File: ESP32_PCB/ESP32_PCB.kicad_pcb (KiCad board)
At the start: 2 copper layers, 40 x 40 mm, 30 parts, among them J1 USB_C_Receptacle, J2 ESC1, J3 ESC2, U2 H3LIS331DL, U3 AP2112K-3.3, U4 TPS54302, U5 ESP32-S3-MINI-1U

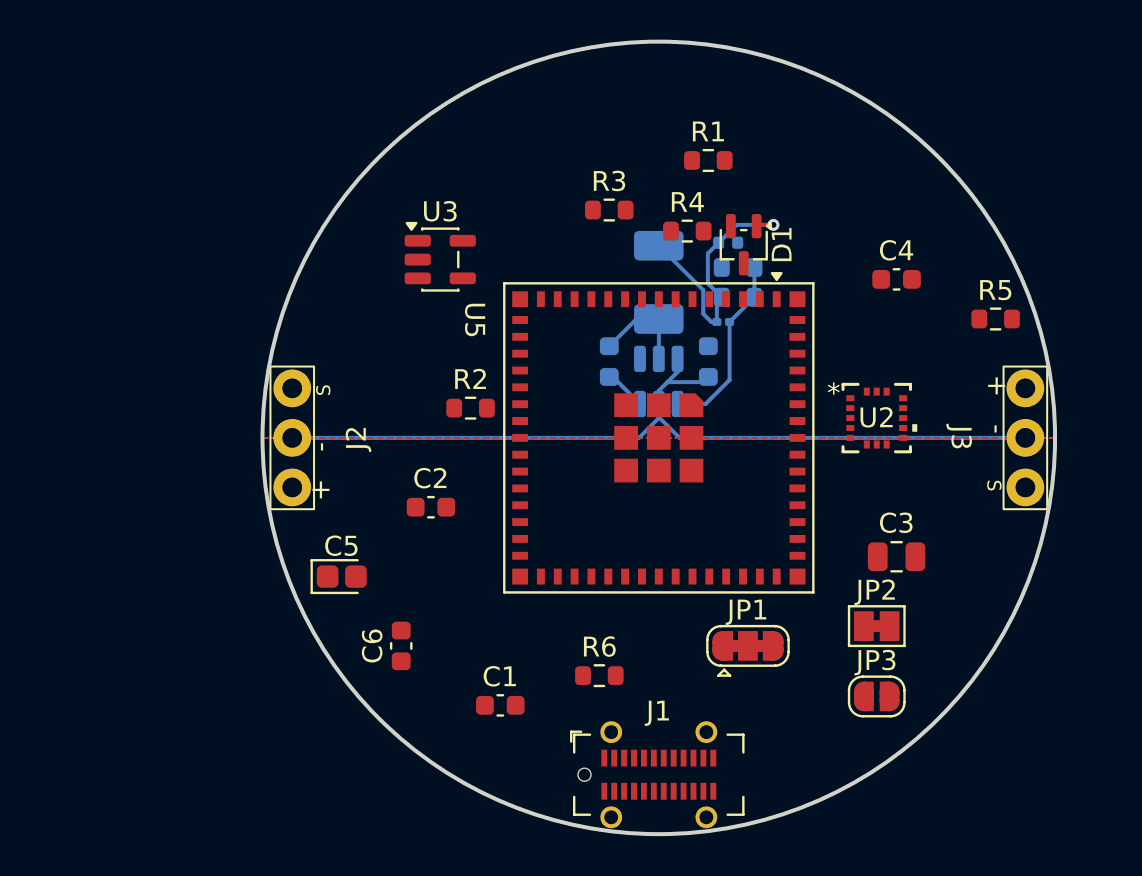
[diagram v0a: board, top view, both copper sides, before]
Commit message: fix pin assignments and add en and boot jumper
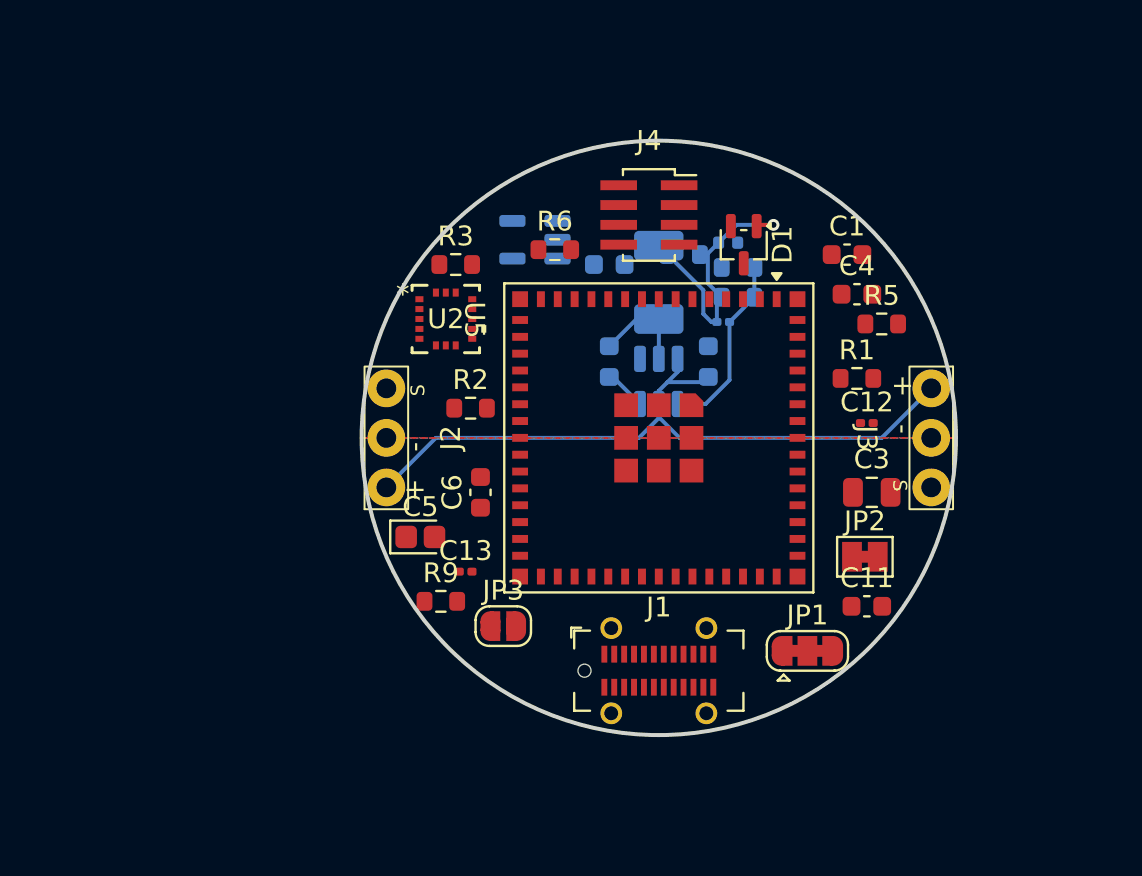
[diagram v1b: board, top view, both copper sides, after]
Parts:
- added C11: 22uF, Capacitor_SMD:C_0603_1608Metric, F.Cu at (160.5, 108.5)
- added C12: 1uF, Capacitor_SMD:C_0201_0603Metric, F.Cu at (160.5, 99.2)
- added C13: 0.1uF, Capacitor_SMD:C_0201_0603Metric, F.Cu at (140.2, 106.8)
- added J4: Conn_02x04_Counter_Clockwise, Connector_PinSocket_1.00mm:PinSocket_2x04_P1.00mm_Vertical_SMD, F.Cu at (149.5, 88.8)
- added R9: 10k, Resistor_SMD:R_0603_1608Metric, F.Cu at (139.0, 108.2)
- C2, R4, U3: moved to B.Cu
- C4: value 100nF -> .1uF
- moved C1 28.7 mm to (159.5, 90.8)
- moved U2 22.3 mm to (139.2, 94.0)
- moved R6 21.6 mm to (144.8, 90.5)
- moved JP3 19.2 mm to (142.2, 109.5)
- moved C2 15.2 mm to (147.5, 91.2), turned to 180 degrees
- moved R1 13.3 mm to (160.0, 97.0)
- moved C6 8.72 mm to (141.0, 102.8)
- moved R3 8.22 mm to (139.8, 91.2)
- moved R5 5.76 mm to (161.2, 94.2)
- moved J1 5.25 mm to (150.0, 111.8)
- moved U3 4.88 mm to (143.8, 90.0), turned to 180 degrees
- moved J2 4.75 mm to (136.2, 100.0)
- moved J3 4.75 mm to (163.8, 100.0)
- moved C5 4.44 mm to (138.0, 105.0)
- moved JP2 3.55 mm to (160.4, 106.0)
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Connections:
- J2 pad 1: /S1 -> VBATT
- J2 pad 2: VBATT -> GNDREF
- J2 pad 3: GNDREF -> /S1
- J3 pad 1: /S2 -> VBATT
- J3 pad 2: VBATT -> GNDREF
- J3 pad 3: GNDREF -> /S2
- U5 pad 19: unconnected-(U5-IO15-Pad19) -> GNDREF
- U5 pad 20: unconnected-(U5-IO16-Pad20) -> GNDREF
- U5 pad 4: unconnected-(U5-IO0-Pad4) -> /BOOT
- U5 pad 45: unconnected-(U5-EN-Pad45) -> /EN
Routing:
- net VBATT: track 44.1 -> 36.6 mm
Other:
- board size 40 x 40 mm -> 30 x 30 mm

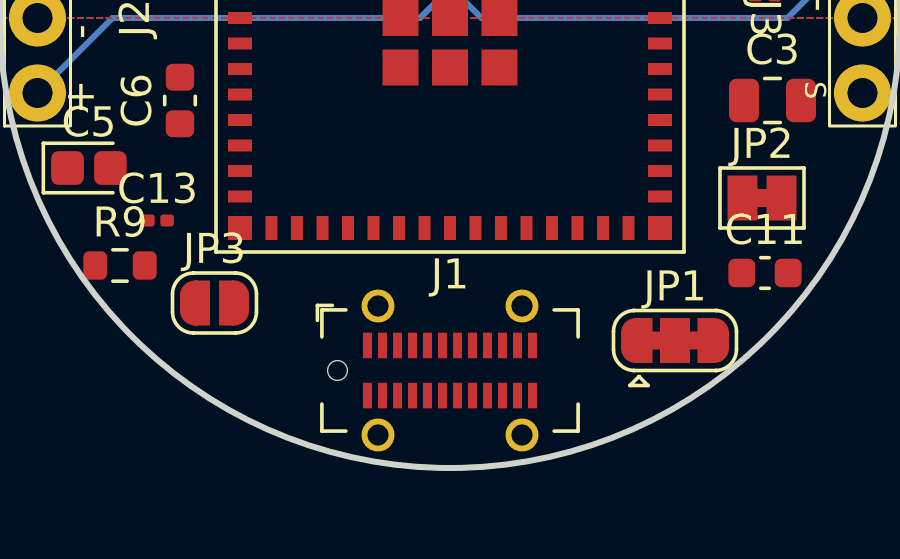
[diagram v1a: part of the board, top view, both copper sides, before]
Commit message: horizontal usb-c
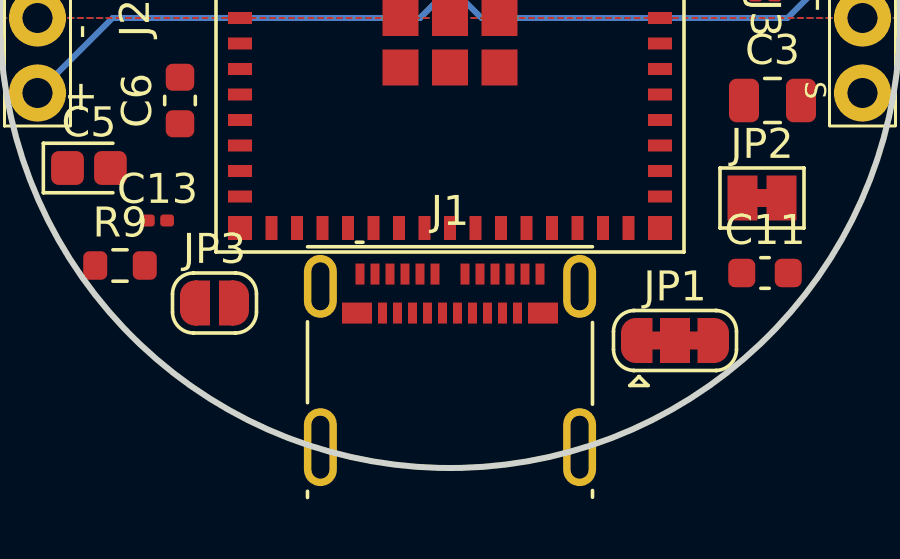
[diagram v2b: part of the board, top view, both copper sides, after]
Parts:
- J1: footprint Connector_USB:USB_C_Receptacle_GCT_USB4115-03-C -> Connector_USB:USB_C_Receptacle_Molex_105450-0101

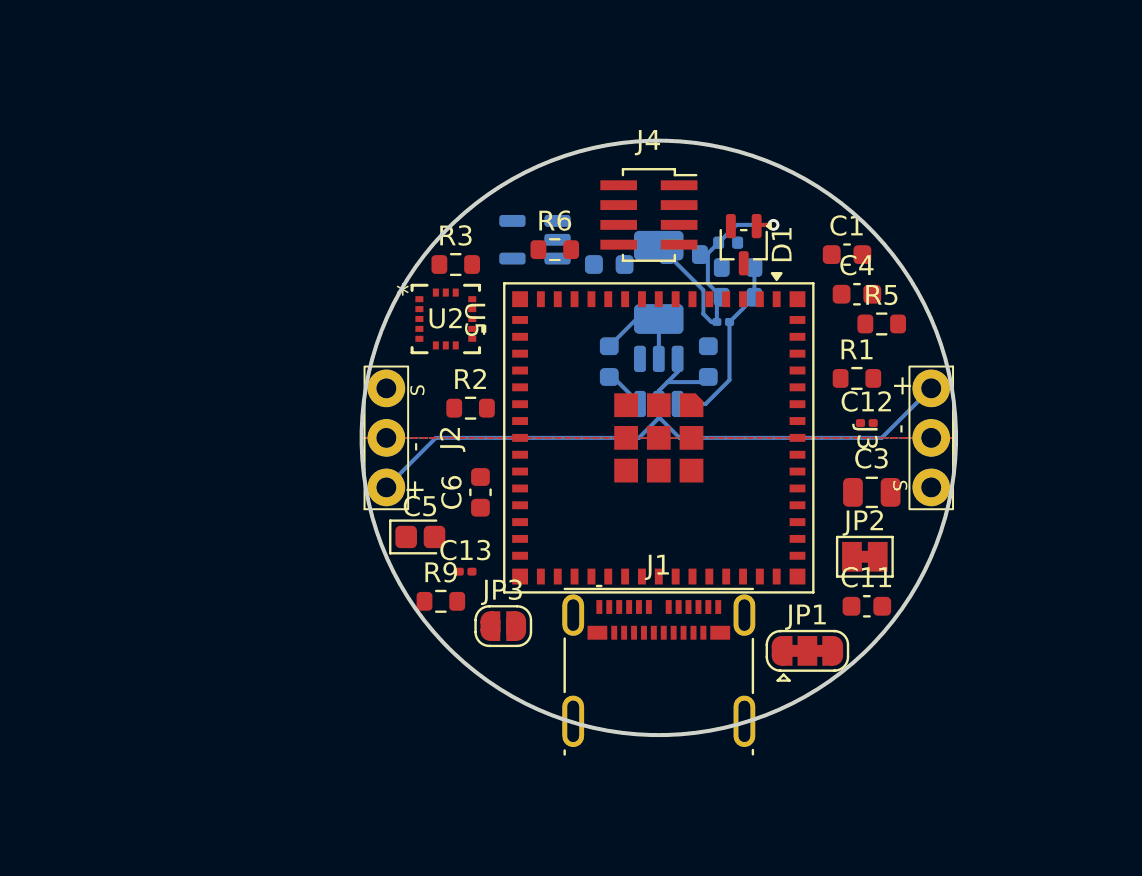
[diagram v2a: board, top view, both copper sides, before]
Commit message: Increase PCB size
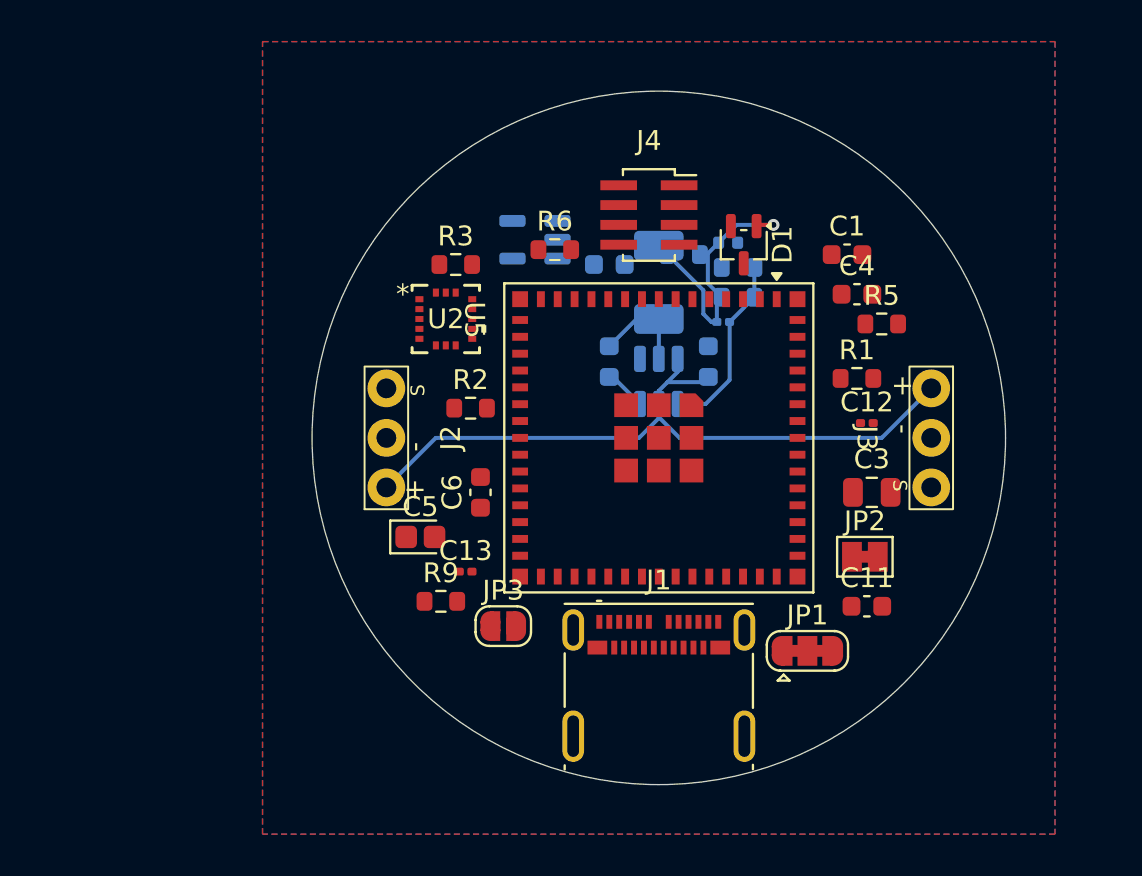
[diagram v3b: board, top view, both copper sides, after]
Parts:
- moved J1 0.75 mm to (150.0, 112.5)
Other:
- board size 30 x 30 mm -> 35 x 35 mm
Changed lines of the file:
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@@
 	(footprint "Connector_USB:USB_C_Receptacle_Molex_105450-0101"
 		(layer "F.Cu")
-		(at 150 111.75)
+		(at 150 112.5)
 		(descr "USB 3.0 3.1 3.2 4.0 Type-C receptable, through-hole mount, SMD, right-angle (https://www.molex.com/pdm_docs/sd/1054500101_sd.pdf)")
 		(tags "USB C Type-C USB3 receptacle SMD")
@@
 			(polygon
 				(pts
-					(xy 153.5 116.075) (xy 146.5 116.075) (xy 146.5 110.445) (xy 153.5 110.445)
+					(xy 153.5 116.825) (xy 146.5 116.825) (xy 146.5 111.195) (xy 153.5 111.195)
 				)
 			)
@@
 	(gr_circle
 		(center 150 100)
-		(end 165 100)
+		(end 150 117.5)
 		(stroke
-			(width 0.2)
-			(type solid)
+			(width 0.05)
+			(type default)
 		)
 		(fill no)
@@
 		(polygon
 			(pts
-				(arc
-					(start 135 100)
-					(mid 165 100)
-					(end 135 100)
-				)
+				(xy 130 80) (xy 170 80) (xy 170 120) (xy 130 120)
 			)
 		)

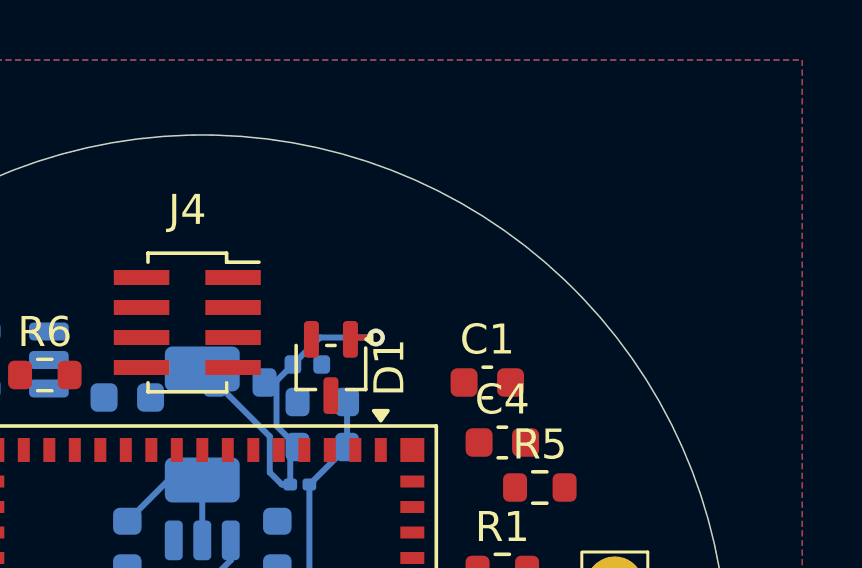
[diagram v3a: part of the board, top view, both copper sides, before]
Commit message: Add LED pins, correct ESC signal pins
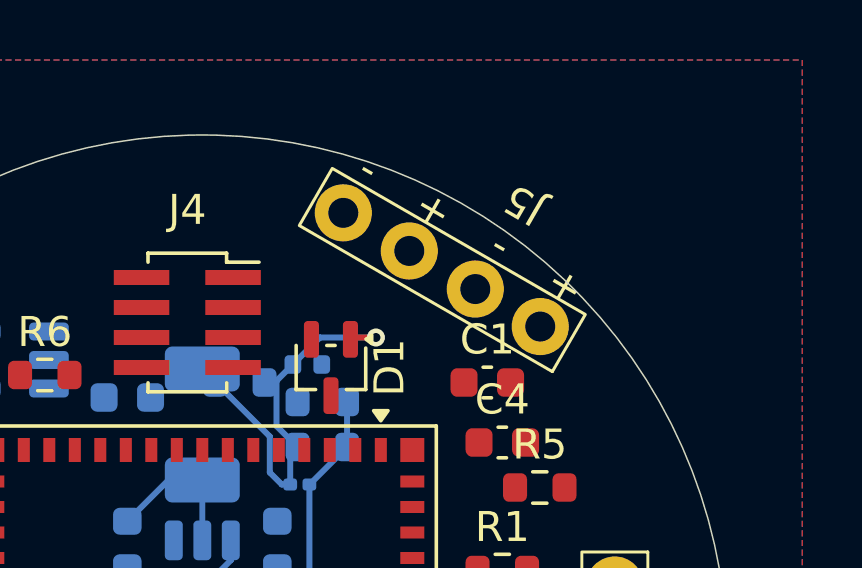
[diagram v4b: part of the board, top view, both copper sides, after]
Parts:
- added J5: LED, ESC_Connectors:4_Pin, F.Cu at (159.1, 87.6)
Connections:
- U5 pad 14: unconnected-(U5-IO10-Pad14) -> /LED
- U5 pad 7: unconnected-(U5-IO3-Pad7) -> /S2
- U5 pad 8: /S2 -> unconnected-(U5-IO4-Pad8)
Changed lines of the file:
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@@
 	(net 64 "unconnected-(U5-IO26-Pad26)")
 	(net 65 "unconnected-(U5-IO12-Pad16)")
-	(net 66 "unconnected-(U5-IO10-Pad14)")
+	(net 66 "unconnected-(U5-IO4-Pad8)")
 	(net 67 "unconnected-(U5-TXD0-Pad39)")
-	(net 68 "unconnected-(U5-IO3-Pad7)")
+	(net 68 "/LED")
 	(net 69 "unconnected-(U5-IO41-Pad37)")
 	(net 70 "unconnected-(U5-IO33-Pad28)")
@@
 			(size 0.8 0.4)
 			(layers "F.Cu" "F.Mask" "F.Paste")
-			(net 68 "unconnected-(U5-IO3-Pad7)")
+			(net 27 "/S2")
 			(pinfunction "IO3")
-			(pintype "bidirectional+no_connect")
+			(pintype "bidirectional")
 		)
 		(pad "8" smd rect
@@
 			(size 0.8 0.4)
 			(layers "F.Cu" "F.Mask" "F.Paste")
-			(net 27 "/S2")
+			(net 66 "unconnected-(U5-IO4-Pad8)")
 			(pinfunction "IO4")
-			(pintype "bidirectional")
+			(pintype "bidirectional+no_connect")
 		)
 		(pad "9" smd rect
@@
 			(size 0.8 0.4)
 			(layers "F.Cu" "F.Mask" "F.Paste")
-			(net 66 "unconnected-(U5-IO10-Pad14)")
+			(net 68 "/LED")
 			(pinfunction "IO10")
-			(pintype "bidirectional+no_connect")
+			(pintype "bidirectional")
 		)
 		(pad "15" smd rect
@@
 		)
 	)
+	(footprint "ESC_Connectors:4_Pin"
+		(layer "F.Cu")
+		(at 159.099852 87.635 150)
+		(property "Reference" "J5"
+			(at 0 3.25 150)
+			(unlocked yes)
+			(layer "F.SilkS")
+			(effects
+				(font
+					(size 1 1)
+					(thickness 0.1)
+				)
+			)
+		)
+		(property "Value" "LED"
+			(at 0 -4.199999 150)
+			(unlocked yes)
+			(layer "F.Fab")
+			(effects
+				(font
+					(size 1 1)
+					(thickness 0.15)
+				)
+			)
+		)
+		(property "Datasheet" "~"
+			(at 0 0 150)
+			(unlocked yes)
+			(layer "F.Fab")
+			(hide yes)
+			(effects
+				(font
+					(size 1 1)
+					(thickness 0.15)
+				)
+			)
+		)
+		(property "Description" "Generic connector, single row, 01x04, script generated (kicad-library-utils/schlib/autogen/connector/)"
+			(at 0 0 150)
+			(unlocked yes)
+			(layer "F.Fab")
+			(hide yes)
+			(effects
+				(font
+					(size 1 1)
+					(thickness 0.15)
+				)
+			)
+		)
+		(property ki_fp_filters "Connector*:*_1x??_*")
+		(sheetname "/")
+		(sheetfile "ESP32_PCB.kicad_sch")
+		(attr smd)
+		(fp_poly
+			(pts
+				(xy -3.6 -1.1) (xy -3.6 1.1) (xy 6.139999 1.100001) (xy 6.139999 -1.1)
+			)
+			(stroke
+				(width 0.1)
+				(type default)
+			)
+			(fill no)
+			(layer "F.SilkS")
+		)
+		(fp_text user "+"
+			(at 2.54 1.524001 150)
+			(unlocked yes)
+			(layer "F.SilkS")
+			(effects
+				(font
+					(size 1 1)
+					(thickness 0.1)
+				)
+			)
+		)
+		(fp_text user "-"
+			(at 5.08 1.523999 150)
+			(unlocked yes)
+			(layer "F.SilkS")
+			(effects
+				(font
+					(size 1 1)
+					(thickness 0.1)
+				)
+			)
+		)
+		(fp_text user "-"
+			(at 0 1.524 150)
+			(unlocked yes)
+			(layer "F.SilkS")
+			(effects
+				(font
+					(size 1 1)
+					(thickness 0.1)
+				)
+			)
+		)
+		(fp_text user "+"
+			(at -2.54 1.524 150)
+			(unlocked yes)
+			(layer "F.SilkS")
+			(effects
+				(font
+					(size 1 1)
+					(thickness 0.1)
+				)
+			)
+		)
+		(fp_text user "4_Pin"
+			(at -0.000001 -2.4 150)
+			(unlocked yes)
+			(layer "F.Fab")
+			(effects
+				(font
+					(size 1 1)
+					(thickness 0.15)
+				)
+			)
+		)
+		(pad "1" thru_hole circle
+			(at -2.5 0 150)
+			(size 1.905 1.905)
+			(drill 1)
+			(layers "*.Cu" "*.Mask")
+			(remove_unused_layers no)
+			(net 68 "/LED")
+			(pinfunction "Pin_1")
+			(pintype "passive")
+		)
+		(pad "2" thru_hole circle
+			(at 0 0 150)
+			(size 1.905 1.905)
+			(drill 1)
+			(layers "*.Cu" "*.Mask")
+			(remove_unused_layers no)
+			(net 2 "GNDREF")
+			(pinfunction "Pin_2")
+			(pintype "passive")
+		)
+		(pad "3" thru_hole circle
+			(at 2.539999 -0.000001 150)
+			(size 1.905 1.905)
+			(drill 1)
+			(layers "*.Cu" "*.Mask")
+			(remove_unused_layers no)
+			(net 68 "/LED")
+			(pinfunction "Pin_3")
+			(pintype "passive")
+		)
+		(pad "4" thru_hole circle
+			(at 5.079999 -0.000001 150)
+			(size 1.905 1.905)
+			(drill 1)
+			(layers "*.Cu" "*.Mask")
+			(remove_unused_layers no)
+			(net 2 "GNDREF")
+			(pinfunction "Pin_4")
+			(pintype "passive")
+		)
+		(zone
+			(net 0)
+			(net_name "")
+			(layer "F.SilkS")
+			(hatch edge 0.5)
+			(connect_pads
+				(clearance 0)
+			)
+			(min_thickness 0.25)
+			(filled_areas_thickness no)
+			(keepout
+				(tracks allowed)
+				(vias allowed)
+				(pads not_allowed)
+				(copperpour allowed)
+				(footprints not_allowed)
+			)
+			(placement
+				(enabled no)
+				(sheetname "")
+			)
+			(fill
+				(thermal_gap 0.5)
+				(thermal_bridge_width 0.5)
+			)
+			(polygon
+				(pts
+					(xy 161.630941 90.251026) (xy 153.369059 85.481026) (xy 154.369059 83.748974) (xy 162.630941 88.518975)
+				)
+			)
+		)
+		(embedded_fonts no)
+	)
 	(footprint "Capacitor_SMD:C_0603_1608Metric"
 		(layer "F.Cu")
@@
 			(layers "*.Cu" "*.Mask")
 			(remove_unused_layers no)
-			(net 12 "unconnected-(J1-SHIELD-PadS1)_1")
+			(net 24 "unconnected-(J1-SHIELD-PadS1)_3")
 			(pinfunction "SHIELD")
 			(pintype "passive+no_connect")
@@
 			(layers "*.Cu" "*.Mask")
 			(remove_unused_layers no)
-			(net 18 "unconnected-(J1-SHIELD-PadS1)_2")
+			(net 11 "unconnected-(J1-SHIELD-PadS1)")
 			(pinfunction "SHIELD")
 			(pintype "passive+no_connect")
@@
 			(layers "*.Cu" "*.Mask")
 			(remove_unused_layers no)
-			(net 24 "unconnected-(J1-SHIELD-PadS1)_3")
+			(net 18 "unconnected-(J1-SHIELD-PadS1)_2")
 			(pinfunction "SHIELD")
 			(pintype "passive+no_connect")
@@
 			(layers "*.Cu" "*.Mask")
 			(remove_unused_layers no)
-			(net 11 "unconnected-(J1-SHIELD-PadS1)")
+			(net 12 "unconnected-(J1-SHIELD-PadS1)_1")
 			(pinfunction "SHIELD")
 			(pintype "passive+no_connect")
